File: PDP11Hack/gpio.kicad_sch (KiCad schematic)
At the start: 11 parts, among them J4000_1 Conn_01x20, U1 74HCT04, U4000_1 WDC65C22, U5000_1 74LS30, U5000_2 74HCT138

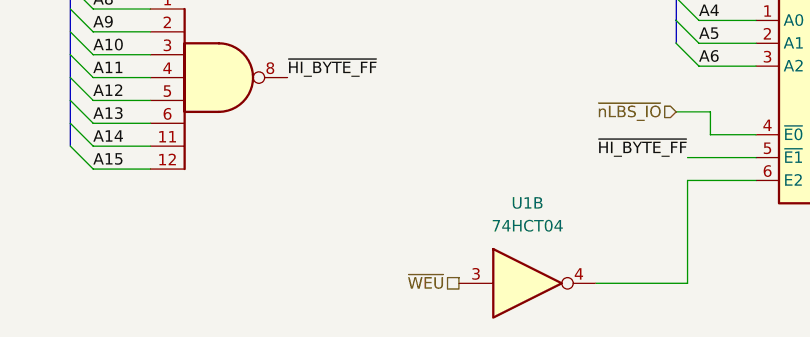
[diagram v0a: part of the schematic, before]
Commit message: Corrections thanks to Peter Schranz on VCFED
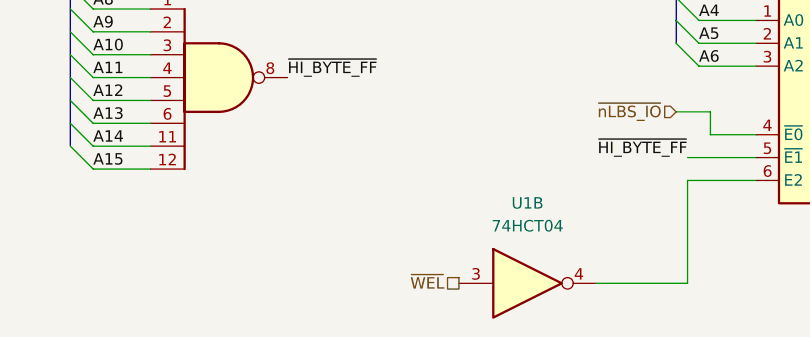
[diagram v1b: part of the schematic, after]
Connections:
- net ~{WEU} is gone; now on net ~{WEL}: U1.3
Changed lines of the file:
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@@
 		)
 	)
-	(hierarchical_label "~{WEU}"
+	(hierarchical_label "~{WEL}"
 		(shape passive)
 		(at 77.47 182.88 180)
@@
 		(on_board yes)
 		(dnp no)
-		(property "Reference" "#PWR039"
+		(property "Reference" "#PWR037"
 			(at 120.65 182.88 0)
 			(effects
@@
 			(project "Modular DCJ11"
 				(path "/264d9b66-53d1-4564-94e8-42c7c0bb6a66/d34c939f-f534-42f5-b646-45de02ff21f9"
-					(reference "#PWR039")
+					(reference "#PWR037")
 					(unit 1)
 				)
@@
 		(on_board yes)
 		(dnp no)
-		(property "Reference" "#PWR040"
+		(property "Reference" "#PWR038"
 			(at 138.43 115.57 0)
 			(effects
@@
 			(project "Modular DCJ11"
 				(path "/264d9b66-53d1-4564-94e8-42c7c0bb6a66/d34c939f-f534-42f5-b646-45de02ff21f9"
-					(reference "#PWR040")
+					(reference "#PWR038")
 					(unit 1)
 				)
@@
 		(on_board yes)
 		(dnp no)
-		(property "Reference" "#PWR042"
+		(property "Reference" "#PWR040"
 			(at 264.16 156.21 0)
 			(effects
@@
 			(project "Modular DCJ11"
 				(path "/264d9b66-53d1-4564-94e8-42c7c0bb6a66/d34c939f-f534-42f5-b646-45de02ff21f9"
-					(reference "#PWR042")
+					(reference "#PWR040")
 					(unit 1)
 				)
@@
 		(on_board yes)
 		(dnp no)
-		(property "Reference" "#PWR041"
+		(property "Reference" "#PWR039"
 			(at 264.16 146.05 0)
 			(effects
@@
 			(project "Modular DCJ11"
 				(path "/264d9b66-53d1-4564-94e8-42c7c0bb6a66/d34c939f-f534-42f5-b646-45de02ff21f9"
-					(reference "#PWR041")
+					(reference "#PWR039")
 					(unit 1)
 				)
@@
 		(on_board yes)
 		(dnp no)
-		(property "Reference" "#PWR038"
+		(property "Reference" "#PWR036"
 			(at 120.65 152.4 0)
 			(effects
@@
 			(project "Modular DCJ11"
 				(path "/264d9b66-53d1-4564-94e8-42c7c0bb6a66/d34c939f-f534-42f5-b646-45de02ff21f9"
-					(reference "#PWR038")
-					(unit 1)
-				)
+					(reference "#PWR036")
+					(unit 1)
+				)

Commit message: Last update, PCB creation ready
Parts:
- removed J4000_1: Conn_01x20, Alius_6502:20pin header, symbol Connector_Generic:Conn_01x20
- added J4000_1: Conn_02x14_Odd_Even, Connector_PinHeader_2.54mm:PinHeader_2x14_P2.54mm_Vertical, symbol Connector_Generic:Conn_02x14_Odd_Even
- U1: footprint (none) -> Package_DIP:DIP-14_W7.62mm
- U4000_1: footprint Alius_6502:40-pin-DIP -> Package_DIP:DIP-40_W15.24mm
- U5000_2: footprint (none) -> Package_DIP:DIP-16_W7.62mm
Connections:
- net GND: now also J4000_1.20 (Pin_20), J4000_1.24 (Pin_24)
- net VCC: now also J4000_1.10 (Pin_10), J4000_1.14 (Pin_14)
- net at U4000_1.10 (PB0): now also J4000_1.11 (Pin_11)
- net at U4000_1.11 (PB1): now also J4000_1.9 (Pin_9)
- net at U4000_1.12 (PB2): now also J4000_1.7 (Pin_7)
- net at U4000_1.13 (PB3): now also J4000_1.5 (Pin_5)
- net at U4000_1.14 (PB4): now also J4000_1.3 (Pin_3)
- net at U4000_1.15 (PB5): now also J4000_1.1 (Pin_1)
- net at U4000_1.16 (PB6): now also J4000_1.2 (Pin_2)
- net at U4000_1.17 (PB7): now also J4000_1.4 (Pin_4)
- net at U4000_1.18 (CB1): now also J4000_1.6 (Pin_6)
- net at U4000_1.19 (CB2): now also J4000_1.8 (Pin_8)
- net at U4000_1.2 (PA0): now also J4000_1.27 (Pin_27)
- net at U4000_1.3 (PA1): now also J4000_1.25 (Pin_25)
- net at U4000_1.39 (CA2): now also J4000_1.26 (Pin_26)
- net at U4000_1.4 (PA2): now also J4000_1.23 (Pin_23)
- net at U4000_1.40 (CA1): now also J4000_1.28 (Pin_28)
- net at U4000_1.5 (PA3): now also J4000_1.21 (Pin_21)
- net at U4000_1.6 (PA4): now also J4000_1.19 (Pin_19)
- net at U4000_1.7 (PA5): now also J4000_1.17 (Pin_17)
- net at U4000_1.8 (PA6): now also J4000_1.15 (Pin_15)
- net at U4000_1.9 (PA7): now also J4000_1.13 (Pin_13)
- no-connect marks 9 -> 11
